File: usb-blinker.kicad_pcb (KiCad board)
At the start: 2 copper layers, 28.4 x 13 mm, 12 parts, among them J1 USB_C_Receptacle_PowerOnly_6P, U1 TLC555xPW

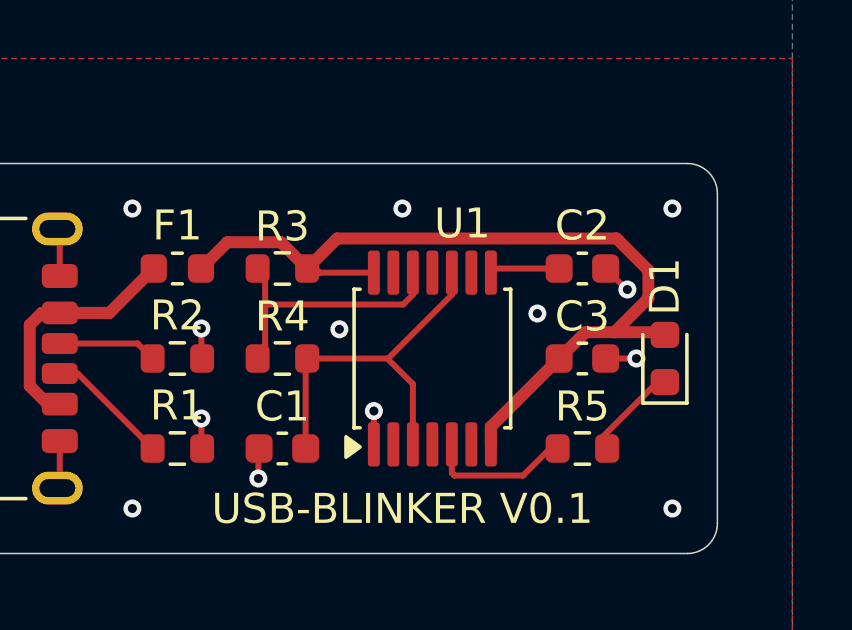
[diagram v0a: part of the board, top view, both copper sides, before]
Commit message: edited pcb traces
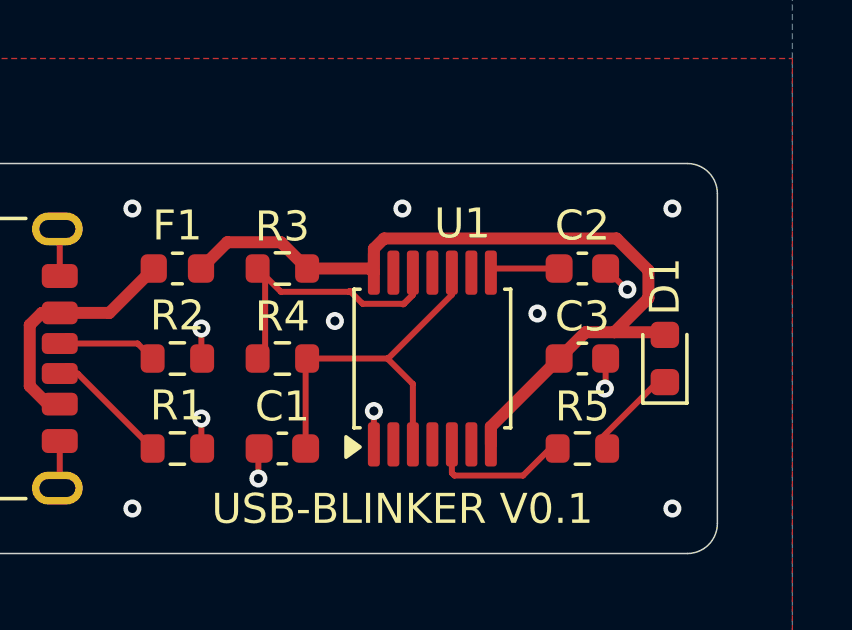
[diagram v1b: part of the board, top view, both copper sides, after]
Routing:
- net +5V: track 29.3 -> 27.9 mm
- net Net-(U1-DISCH): track 8.90 -> 10.1 mm
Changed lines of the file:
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@@
-	)
-	(segment
-		(start 154.8 90)
-		(end 153.775 90)
-		(width 0.2)
-		(layer "F.Cu")
-		(net 1)
 	)
 	(segment
@@
 	)
 	(segment
+		(start 153.775 90.975)
+		(end 153.775 90)
+		(width 0.2)
+		(layer "F.Cu")
+		(net 1)
+	)
+	(segment
 		(start 140.3 92.95)
 		(end 140.325 92.975)
@@
 	)
 	(segment
+		(start 153.75 91)
+		(end 153.775 90.975)
+		(width 0.2)
+		(layer "F.Cu")
+		(net 1)
+	)
+	(segment
 		(start 135.58 92.75)
 		(end 135.58 94.24)
@@
 	)
 	(via
-		(at 154.8 90)
-		(size 0.6)
-		(drill 0.3)
-		(layers "F.Cu" "B.Cu")
-		(free yes)
-		(net 1)
-	)
-	(via
-		(at 144.9 89.025)
+		(at 153.75 91)
+		(size 0.6)
+		(drill 0.3)
+		(layers "F.Cu" "B.Cu")
+		(free yes)
+		(net 1)
+	)
+	(via
+		(at 144.75 88.75)
 		(size 0.6)
 		(drill 0.3)
@@
 	)
 	(segment
-		(start 147.024999 88.2)
-		(end 142.425 88.2)
-		(width 0.2)
-		(layer "F.Cu")
-		(net 4)
-	)
-	(segment
-		(start 147.35 87.1375)
+		(start 142.175 87)
+		(end 142.951 87.776)
+		(width 0.2)
+		(layer "F.Cu")
+		(net 4)
+	)
+	(segment
+		(start 147.048999 88.176)
 		(end 147.35 87.874999)
+		(width 0.2)
+		(layer "F.Cu")
+		(net 4)
+	)
+	(segment
+		(start 142.951 87.776)
+		(end 145.224 87.776)
+		(width 0.2)
+		(layer "F.Cu")
+		(net 4)
+	)
+	(segment
+		(start 145.224 87.776)
+		(end 145.25 87.75)
+		(width 0.2)
+		(layer "F.Cu")
+		(net 4)
+	)
+	(segment
+		(start 145.25 87.75)
+		(end 145.676 88.176)
 		(width 0.2)
 		(layer "F.Cu")
@@
 	)
 	(segment
+		(start 147.35 87.874999)
+		(end 147.35 87.1375)
+		(width 0.2)
+		(layer "F.Cu")
+		(net 4)
+	)
+	(segment
 		(start 142.425 89.75)
 		(end 142.175 90)
@@
 	)
 	(segment
+		(start 145.676 88.176)
+		(end 147.048999 88.176)
+		(width 0.2)
+		(layer "F.Cu")
+		(net 4)
+	)
+	(segment
 		(start 147.35 87.874999)
 		(end 147.024999 88.2)
@@
 	)
 	(segment
-		(start 143.825 87)
-		(end 144.826 85.999)
-		(width 0.4)
-		(layer "F.Cu")
-		(net 15)
-	)
-	(segment
-		(start 144.826 85.999)
-		(end 154.140532 85.999)
-		(width 0.4)
-		(layer "F.Cu")
-		(net 15)
-	)
-	(segment
 		(start 151.975 90)
 		(end 152.225 90)
@@
 	)
 	(segment
+		(start 145.9125 87)
+		(end 146.05 87.1375)
+		(width 0.4)
+		(layer "F.Cu")
+		(net 15)
+	)
+	(segment
 		(start 144.075 87)
 		(end 144.1 87)
@@
 	)
 	(segment
+		(start 146.389708 85.999)
+		(end 154.140532 85.999)
+		(width 0.4)
+		(layer "F.Cu")
+		(net 15)
+	)
+	(segment
 		(start 154.067364 89.124)
 		(end 153.101 89.124)
@@
 	)
 	(segment
+		(start 143.825 87)
+		(end 145.9125 87)
+		(width 0.4)
+		(layer "F.Cu")
+		(net 15)
+	)
+	(segment
+		(start 146.05 86.338708)
+		(end 146.389708 85.999)
+		(width 0.4)
+		(layer "F.Cu")
+		(net 15)
+	)
+	(segment
+		(start 146.05 87.1375)
+		(end 146.05 86.338708)
+		(width 0.4)
+		(layer "F.Cu")
+		(net 15)
+	)
+	(segment
 		(start 140.2875 87)
 		(end 141.1635 86.124)
@@
 	)
 	(segment
-		(start 144.2375 87.1375)
-		(end 146.05 87.1375)
-		(width 0.2)
-		(layer "F.Cu")
-		(net 15)
-	)
-	(segment
 		(start 153.101 89.124)
 		(end 152.225 90)
@@
 		(layer "F.Cu")
 		(net 15)
-	)
-	(segment
-		(start 144.1 87)
-		(end 144.2375 87.1375)
-		(width 0.2)
-		(layer "F.Cu")
-		(net 15)
